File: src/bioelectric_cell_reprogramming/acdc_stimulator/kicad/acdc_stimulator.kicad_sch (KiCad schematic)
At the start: 76 parts, among them IC1 AD9833BRM-REEL7, IC3 AD5122BCPZ10-RL7, J1 USB_C_Receptacle_USB2.0_14P, J2 Conn_01x02_Socket, J3 Conn_ARM_SWD_TagConnect_TC203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, J4 Screw_Terminal_01x02, J5 Conn_ARM_SWD_TagConnect_TC203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, J6 USB_C_Receptacle_USB2.0_14P, Q10 BSZ096N10LS5ATMA1, SW1 SW_Push, SW2 SW_SPDT, SW3 SW_Push, SW4 SW_SPDT, U1 STM32G431CBU3, U2 USBLC6-2SC6, U3 AMS1117-3.3, U6 STM32G473RCTx, U7 USBLC6-2SC6, Y1 16Mhz, Y2 16Mhz

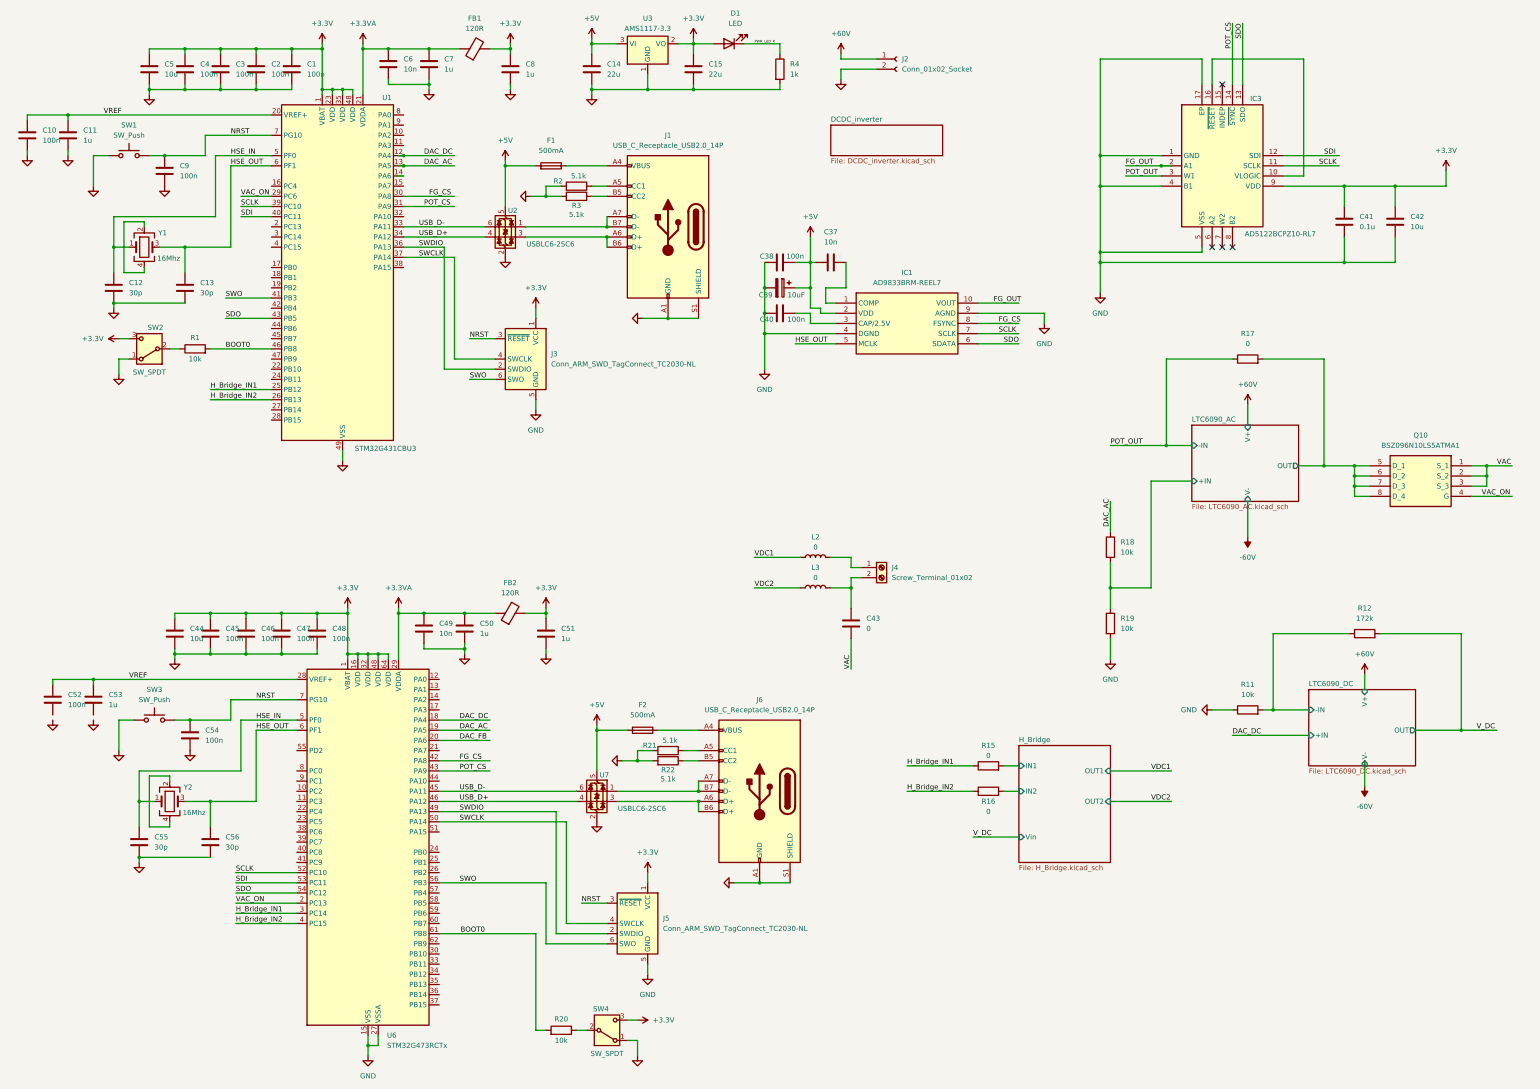
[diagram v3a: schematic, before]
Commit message: ci: added error op amp to ADC
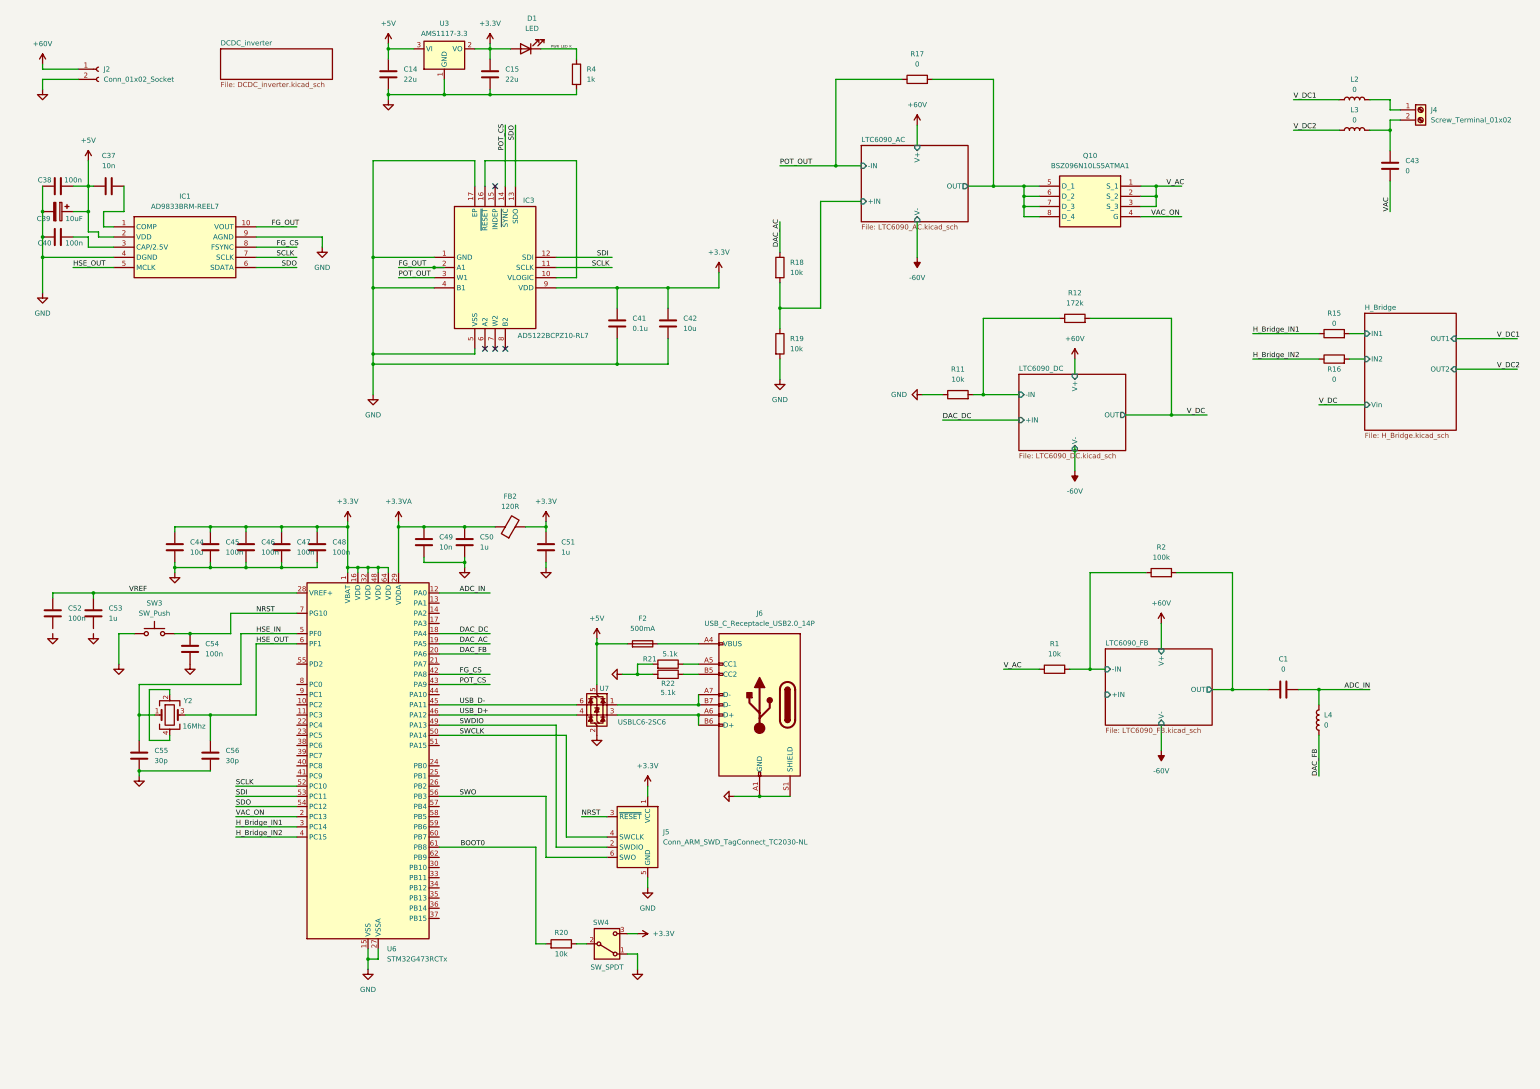
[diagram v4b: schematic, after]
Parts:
- removed C10, C9: 100n, Capacitor_SMD:C_0402_1005Metric, symbol Device:C
- removed C11: 1u, Capacitor_SMD:C_0402_1005Metric, symbol Device:C
- removed C12, C13: 30p, symbol Device:C
- removed C2, C3, C4: 100n, symbol Device:C
- removed C5: 10u, symbol Device:C
- removed C6: 10n, symbol Device:C
- removed C7, C8: 1u, symbol Device:C
- removed F1: 500mA, Fuse:Fuse_0603_1608Metric, symbol Device:Fuse
- removed FB1: 120R, symbol Device:FerriteBead
- removed J1: USB_C_Receptacle_USB2.0_14P, Connector_USB:USB_C_Receptacle_GCT_USB4105-xx-A_16P_TopMnt_Horizontal, symbol Connector:USB_C_Receptacle_USB2.0_14P
- removed J3: Conn_ARM_SWD_TagConnect_TC2030-NL, Connector:Tag-Connect_TC2030-IDC-NL_2x03_P1.27mm_Vertical, symbol Connector:Conn_ARM_SWD_TagConnect_TC2030-NL
- removed R3: 5.1k, Resistor_SMD:R_0603_1608Metric, symbol Device:R
- removed SW1: SW_Push, Button_Switch_THT:SW_PUSH-12mm_Wuerth-430476085716, symbol Switch:SW_Push
- removed SW2: SW_SPDT, symbol Switch:SW_SPDT
- removed U1: STM32G431CBU3, Package_DFN_QFN:QFN-48-1EP_7x7mm_P0.5mm_EP5.6x5.6mm, symbol MCU_ST_STM32G4:STM32G431CBUx
- removed U2: USBLC6-2SC6, Package_TO_SOT_SMD:SOT-23-6, symbol Power_Protection:USBLC6-2SC6
- removed Y1: 16Mhz, symbol Device:Crystal_GND24
- added L4: 0, symbol Device:L
- C1: value 100n -> 0
- R2: value 5.1k -> 100k; footprint Resistor_SMD:R_0603_1608Metric -> (none)
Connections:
- net +3.3V: no longer C1.1
- net BOOT0: no longer R1.2
- net DAC_FB: now also L4.1
- net GND: no longer C1.2, R2.2
- net VAC: no longer Q10.1 (S_1), Q10.2 (S_2), Q10.3 (S_3)
- net ADC_IN: now reaches U6.12 (PA0)
- net ADC_IN: now also C1.2, L4.2
- net LTC6090_FB/-IN: now reaches R2.1
- net LTC6090_FB/-IN: now also R1.2
- net V_AC: now reaches R1.1
- net V_AC: now also Q10.1 (S_1), Q10.2 (S_2), Q10.3 (S_3)
- net VDC1 renamed V_DC1
- net VDC2 renamed V_DC2
- new net LTC6090_FB/OUT: C1.1, R2.2
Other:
- added sheet LTC6090_FB (LTC6090_FB.kicad_sch)
- moved on the sheet: C14, C15, C37, C38, C39, C40, C41, C42, C43, C44, C45, C46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
